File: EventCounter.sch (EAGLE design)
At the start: 24 parts, among them J1 CONN_42.54_SCREW, Q1 2N7002, Q3 DMG3404, U7 MCP6041, U8 MCP6041

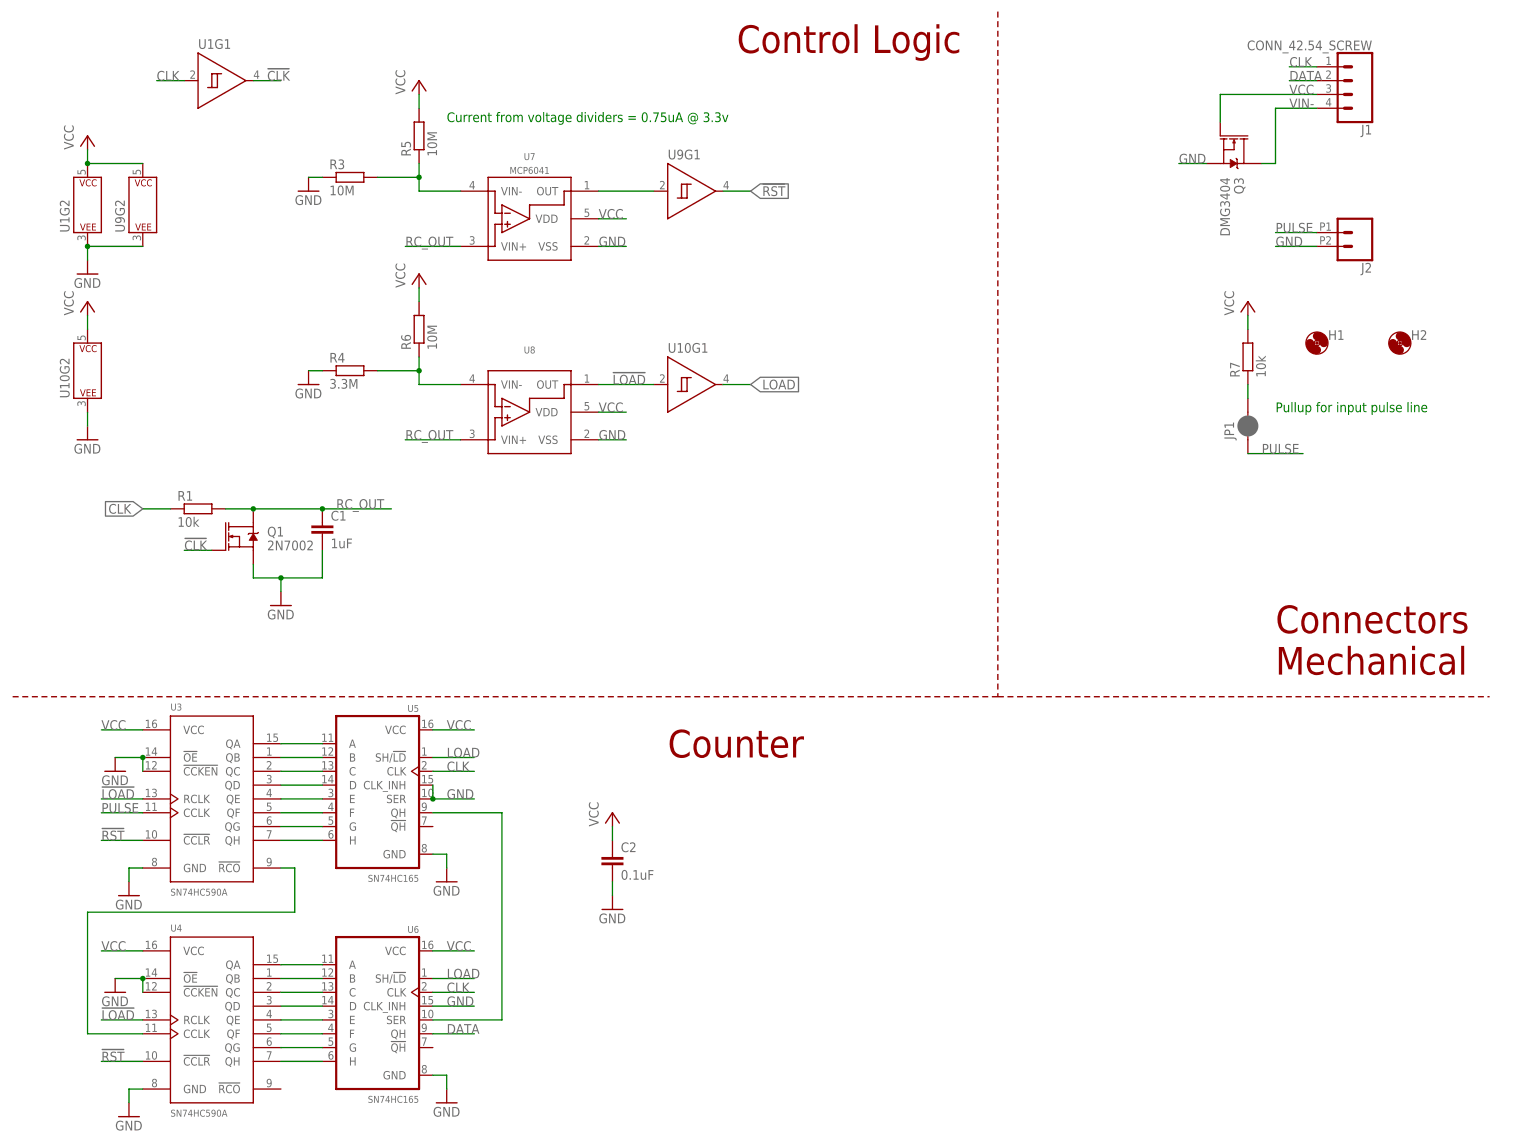
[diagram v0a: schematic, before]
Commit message: Added input signal conditioning, added test script
Added input signal conditioning to fix metastability problem occurring due to excessive rise times due to pullup input
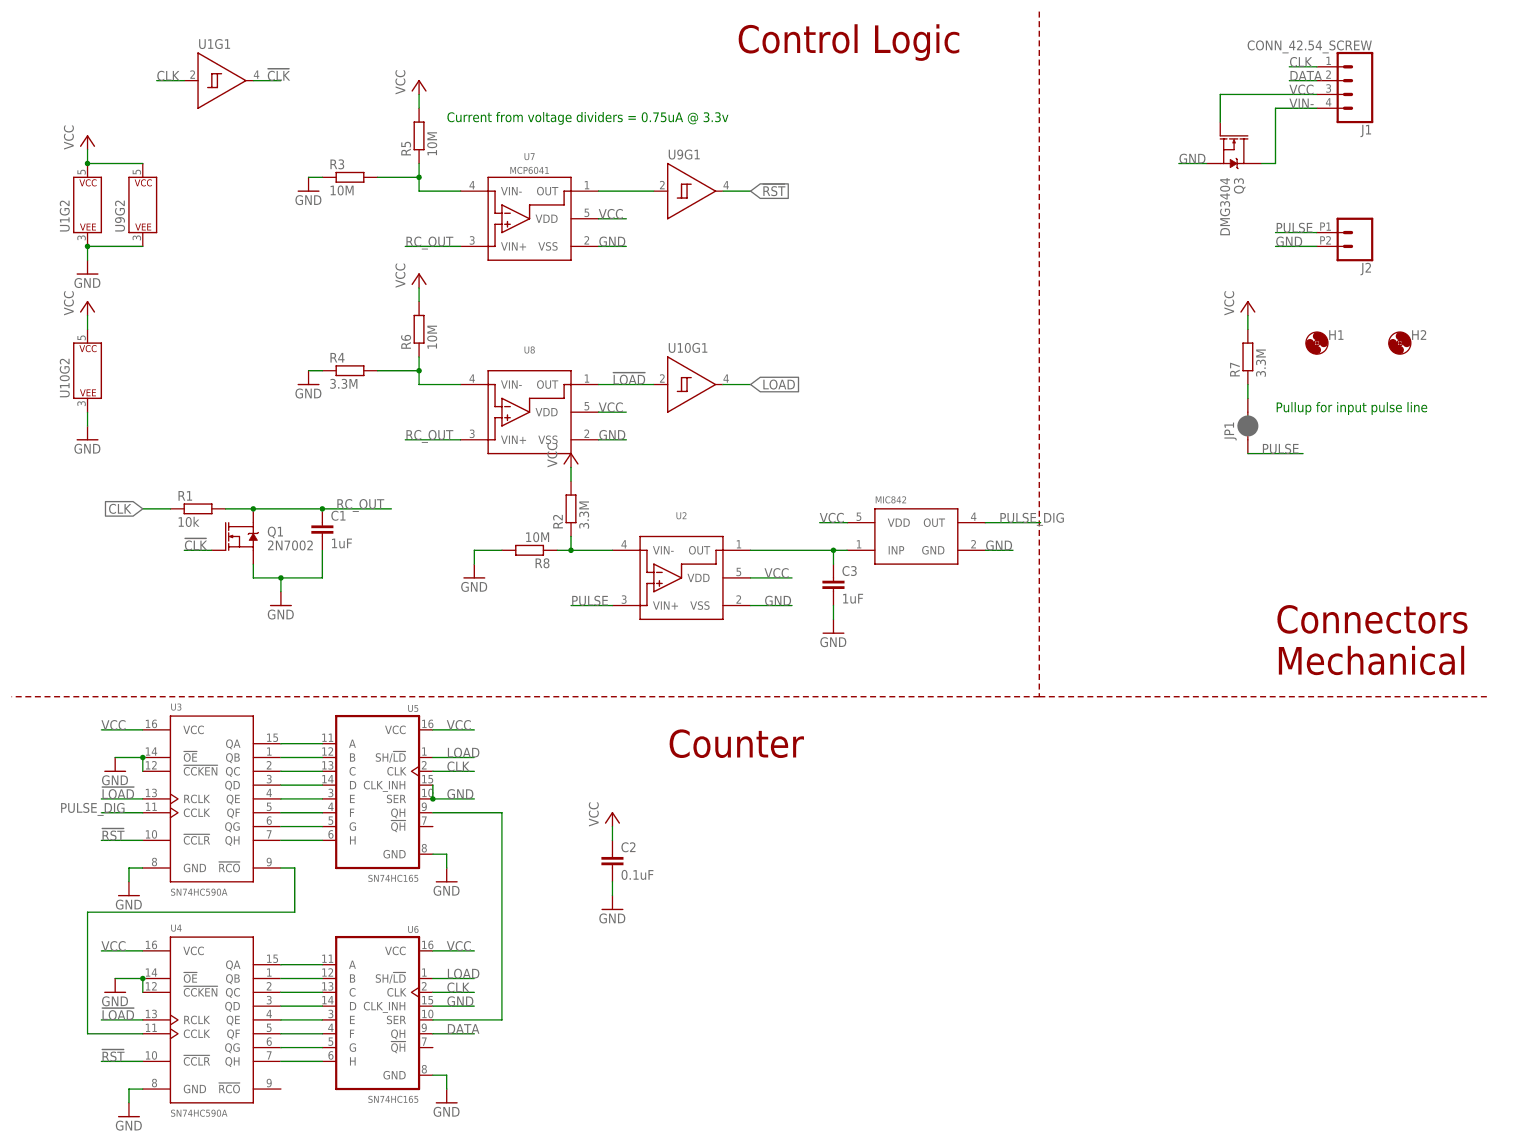
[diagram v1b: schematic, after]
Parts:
- added C3: 1uF, bschulz_passives:C-EUC0603
- added R2: 3.3M, bschulz_passives:R-EU_3.3MR0603
- added R8: 10M, bschulz_passives:R-EU_10MR0603
- added U$1: MIC842H, bschulz:MIC842H
- added U2: MCP6041, bschulz:MCP6041
- R7: value 10k -> 3.3M; device bschulz_passives:R-EU_10KR0603 -> bschulz_passives:R-EU_3.3MR0603
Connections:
- new net N$19: R2.1, R8.1, U2.VIN-
- new net N$24: C3.1, U$1.INP, U2.OUT
- new net PULSE_DIG: U$1.OUT, U3.CCLK
- net GND: now also C3.2, R8.2, U$1.GND, U2.VSS
- net PULSE: now also U2.VIN+; no longer U3.CCLK
- net VCC: now also R2.2, U$1.VDD, U2.VDD

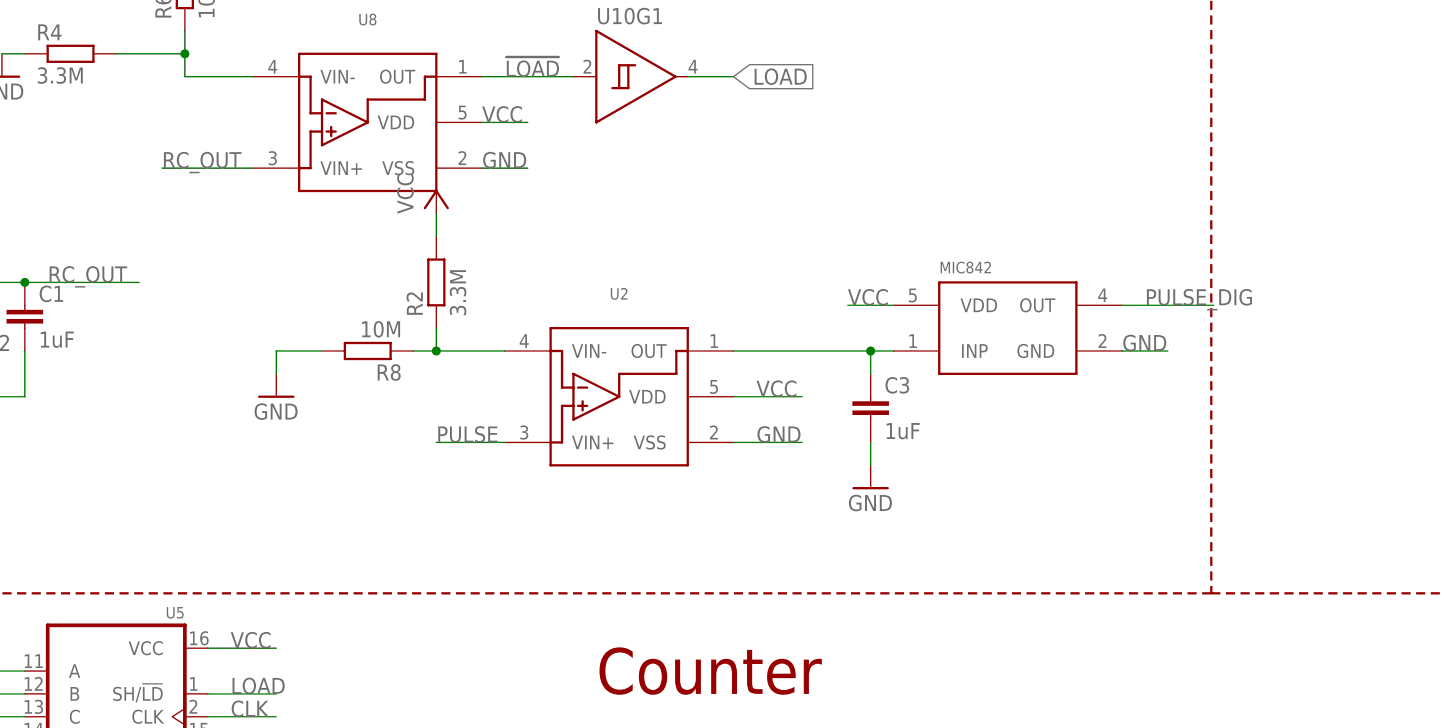
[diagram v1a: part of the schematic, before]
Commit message: Updated part info, license and BOM
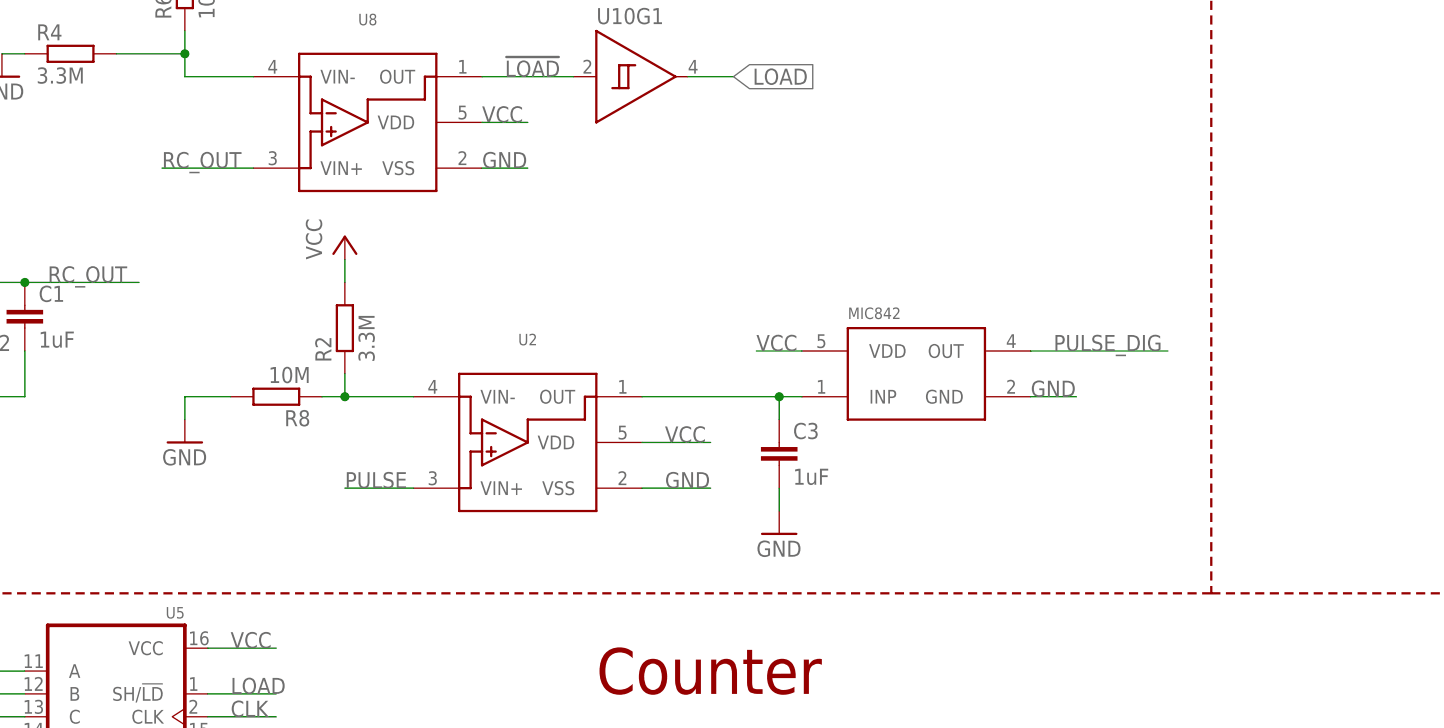
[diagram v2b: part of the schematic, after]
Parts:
- C3: device bschulz_passives:C-EUC0603 -> bschulz_passives:C-EU1UFC0603
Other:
- moved on the sheet: C3, R2, R8, U2
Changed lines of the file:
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@@
 <attribute name="DESIGNER" value="Bobby Schulz"/>
 <attribute name="PROJECT" value="Tally"/>
-<attribute name="REV" value="0.0"/>
+<attribute name="REV" value="0.1"/>
 </part>
 <part name="C2" library="bschulz_passives" deviceset="C-EU" device="C0603" technology="0.1UF" value="0.1uF"/>
@@
 <part name="GND13" library="supply1" library_urn="urn:adsk.eagle:library:371" deviceset="GND" device=""/>
 <part name="U$1" library="bschulz" deviceset="MIC842" device="" technology="H"/>
-<part name="C3" library="bschulz_passives" deviceset="C-EU" device="C0603" value="1uF"/>
+<part name="C3" library="bschulz_passives" deviceset="C-EU" device="C0603" technology="1UF" value="1uF"/>
 <part name="GND14" library="supply1" library_urn="urn:adsk.eagle:library:371" deviceset="GND" device=""/>
 </parts>
@@
 <instance part="GND10" gate="1" x="114.3" y="45.72"/>
 <instance part="P+6" gate="VCC" x="114.3" y="63.5"/>
-<instance part="U2" gate="G$1" x="121.92" y="106.68">
-<attribute name="DISP" x="121.92" y="106.68" size="1.778" layer="96" ratio="15" display="off"/>
+<instance part="U2" gate="G$1" x="111.76" y="101.6">
+<attribute name="DISP" x="111.76" y="101.6" size="1.778" layer="96" ratio="15" display="off"/>
 </instance>
-<instance part="R2" gate="G$1" x="106.68" y="119.38" rot="R90"/>
-<instance part="R8" gate="G$1" x="99.06" y="111.76" rot="R180"/>
-<instance part="P+7" gate="VCC" x="106.68" y="129.54"/>
-<instance part="GND13" gate="1" x="88.9" y="106.68"/>
-<instance part="U$1" gate="G$1" x="167.64" y="114.3"/>
-<instance part="C3" gate="G$1" x="154.94" y="106.68"/>
-<instance part="GND14" gate="1" x="154.94" y="96.52"/>
+<instance part="R2" gate="G$1" x="96.52" y="114.3" rot="R90"/>
+<instance part="R8" gate="G$1" x="88.9" y="106.68" rot="R180"/>
+<instance part="P+7" gate="VCC" x="96.52" y="124.46"/>
+<instance part="GND13" gate="1" x="78.74" y="101.6"/>
+<instance part="U$1" gate="G$1" x="157.48" y="109.22"/>
+<instance part="C3" gate="G$1" x="144.78" y="101.6"/>
+<instance part="GND14" gate="1" x="144.78" y="91.44"/>
 </instances>
 <busses>
@@
 <segment>
 <pinref part="R2" gate="G$1" pin="2"/>
-<wire x1="106.68" y1="124.46" x2="106.68" y2="127" width="0.1524" layer="91"/>
+<wire x1="96.52" y1="119.38" x2="96.52" y2="121.92" width="0.1524" layer="91"/>
 <pinref part="P+7" gate="VCC" pin="VCC"/>
 </segment>
 <segment>
 <pinref part="U2" gate="G$1" pin="VDD"/>
-<wire x1="139.7" y1="106.68" x2="147.32" y2="106.68" width="0.1524" layer="91"/>
-<label x="142.24" y="106.68" size="1.778" layer="95"/>
+<wire x1="129.54" y1="101.6" x2="137.16" y2="101.6" width="0.1524" layer="91"/>
+<label x="132.08" y="101.6" size="1.778" layer="95"/>
 </segment>
 <segment>
 <pinref part="U$1" gate="G$1" pin="VDD"/>
-<wire x1="157.48" y1="116.84" x2="152.4" y2="116.84" width="0.1524" layer="91"/>
-<label x="152.4" y="116.84" size="1.778" layer="95"/>
+<wire x1="147.32" y1="111.76" x2="142.24" y2="111.76" width="0.1524" layer="91"/>
+<label x="142.24" y="111.76" size="1.778" layer="95"/>
 </segment>
 </net>
@@
 <segment>
 <pinref part="GND13" gate="1" pin="GND"/>
-<wire x1="88.9" y1="109.22" x2="88.9" y2="111.76" width="0.1524" layer="91"/>
+<wire x1="78.74" y1="104.14" x2="78.74" y2="106.68" width="0.1524" layer="91"/>
 <pinref part="R8" gate="G$1" pin="2"/>
-<wire x1="88.9" y1="111.76" x2="93.98" y2="111.76" width="0.1524" layer="91"/>
+<wire x1="78.74" y1="106.68" x2="83.82" y2="106.68" width="0.1524" layer="91"/>
 </segment>
 <segment>
 <pinref part="U2" gate="G$1" pin="VSS"/>
-<wire x1="139.7" y1="101.6" x2="147.32" y2="101.6" width="0.1524" layer="91"/>
-<label x="142.24" y="101.6" size="1.778" layer="95"/>
+<wire x1="129.54" y1="96.52" x2="137.16" y2="96.52" width="0.1524" layer="91"/>
+<label x="132.08" y="96.52" size="1.778" layer="95"/>
 </segment>
 <segment>
 <pinref part="U$1" gate="G$1" pin="GND"/>
-<wire x1="182.88" y1="111.76" x2="187.96" y2="111.76" width="0.1524" layer="91"/>
-<label x="182.88" y="111.76" size="1.778" layer="95"/>
+<wire x1="172.72" y1="106.68" x2="177.8" y2="106.68" width="0.1524" layer="91"/>
+<label x="172.72" y="106.68" size="1.778" layer="95"/>
 </segment>
 <segment>
 <pinref part="GND14" gate="1" pin="GND"/>
 <pinref part="C3" gate="G$1" pin="2"/>
-<wire x1="154.94" y1="99.06" x2="154.94" y2="101.6" width="0.1524" layer="91"/>
+<wire x1="144.78" y1="93.98" x2="144.78" y2="96.52" width="0.1524" layer="91"/>
 </segment>
 </net>
@@
 <segment>
 <pinref part="U2" gate="G$1" pin="VIN+"/>
-<wire x1="114.3" y1="101.6" x2="106.68" y2="101.6" width="0.1524" layer="91"/>
-<label x="106.68" y="101.6" size="1.778" layer="95"/>
+<wire x1="104.14" y1="96.52" x2="96.52" y2="96.52" width="0.1524" layer="91"/>
+<label x="96.52" y="96.52" size="1.778" layer="95"/>
 </segment>
 </net>
@@
 <pinref part="U2" gate="G$1" pin="VIN-"/>
 <pinref part="R8" gate="G$1" pin="1"/>
-<wire x1="114.3" y1="111.76" x2="106.68" y2="111.76" width="0.1524" layer="91"/>
+<wire x1="104.14" y1="106.68" x2="96.52" y2="106.68" width="0.1524" layer="91"/>
 <pinref part="R2" gate="G$1" pin="1"/>
-<wire x1="106.68" y1="111.76" x2="104.14" y2="111.76" width="0.1524" layer="91"/>
-<wire x1="106.68" y1="114.3" x2="106.68" y2="111.76" width="0.1524" layer="91"/>
-<junction x="106.68" y="111.76"/>
+<wire x1="96.52" y1="106.68" x2="93.98" y2="106.68" width="0.1524" layer="91"/>
+<wire x1="96.52" y1="109.22" x2="96.52" y2="106.68" width="0.1524" layer="91"/>
+<junction x="96.52" y="106.68"/>
 </segment>
 </net>
@@
 <segment>
 <pinref part="U2" gate="G$1" pin="OUT"/>
-<wire x1="139.7" y1="111.76" x2="154.94" y2="111.76" width="0.1524" layer="91"/>
+<wire x1="129.54" y1="106.68" x2="144.78" y2="106.68" width="0.1524" layer="91"/>
 <pinref part="U$1" gate="G$1" pin="INP"/>
 <pinref part="C3" gate="G$1" pin="1"/>
-<wire x1="154.94" y1="111.76" x2="157.48" y2="111.76" width="0.1524" layer="91"/>
-<wire x1="154.94" y1="109.22" x2="154.94" y2="111.76" width="0.1524" layer="91"/>
-<junction x="154.94" y="111.76"/>
+<wire x1="144.78" y1="106.68" x2="147.32" y2="106.68" width="0.1524" layer="91"/>
+<wire x1="144.78" y1="104.14" x2="144.78" y2="106.68" width="0.1524" layer="91"/>
+<junction x="144.78" y="106.68"/>
 </segment>
 </net>
@@
 <segment>
 <pinref part="U$1" gate="G$1" pin="OUT"/>
-<wire x1="182.88" y1="116.84" x2="193.04" y2="116.84" width="0.1524" layer="91"/>
-<label x="185.42" y="116.84" size="1.778" layer="95"/>
-</segment>
-</net>
+<wire x1="172.72" y1="111.76" x2="187.96" y2="111.76" width="0.1524" layer="91"/>
+<label x="175.26" y="111.76" size="1.778" layer="95"/>
+</segment>
+</net>
